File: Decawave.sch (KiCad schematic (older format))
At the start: 47 parts, among them J1 USB_OTG, J2 USART1, J3 PWR, J4 GPIO, SW1 RESET, U1 STM32L443CCTx_u, U2 MCP1700-3302E_SOT23, X1 JTAG-10

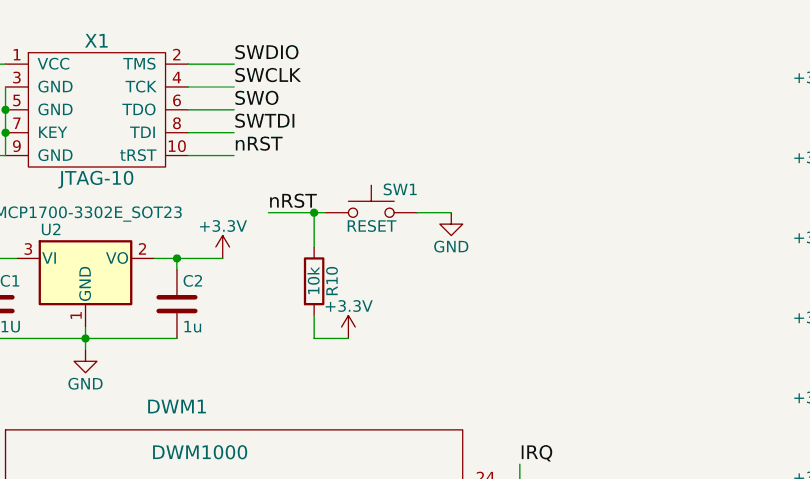
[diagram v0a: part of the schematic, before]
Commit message: adding 100n Cap for nRST
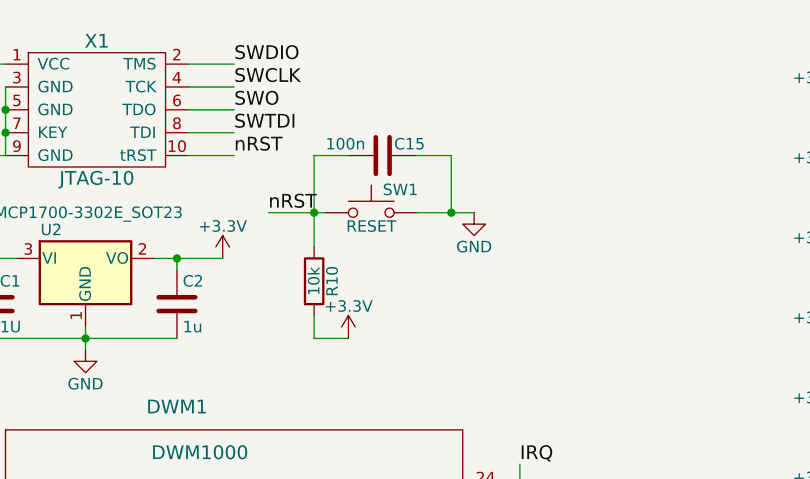
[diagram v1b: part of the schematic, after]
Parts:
- added C15: 100n, Capacitors_SMD:C_0603_HandSoldering, symbol C
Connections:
- net GND: now also C15.1
- net nRST: now also C15.2

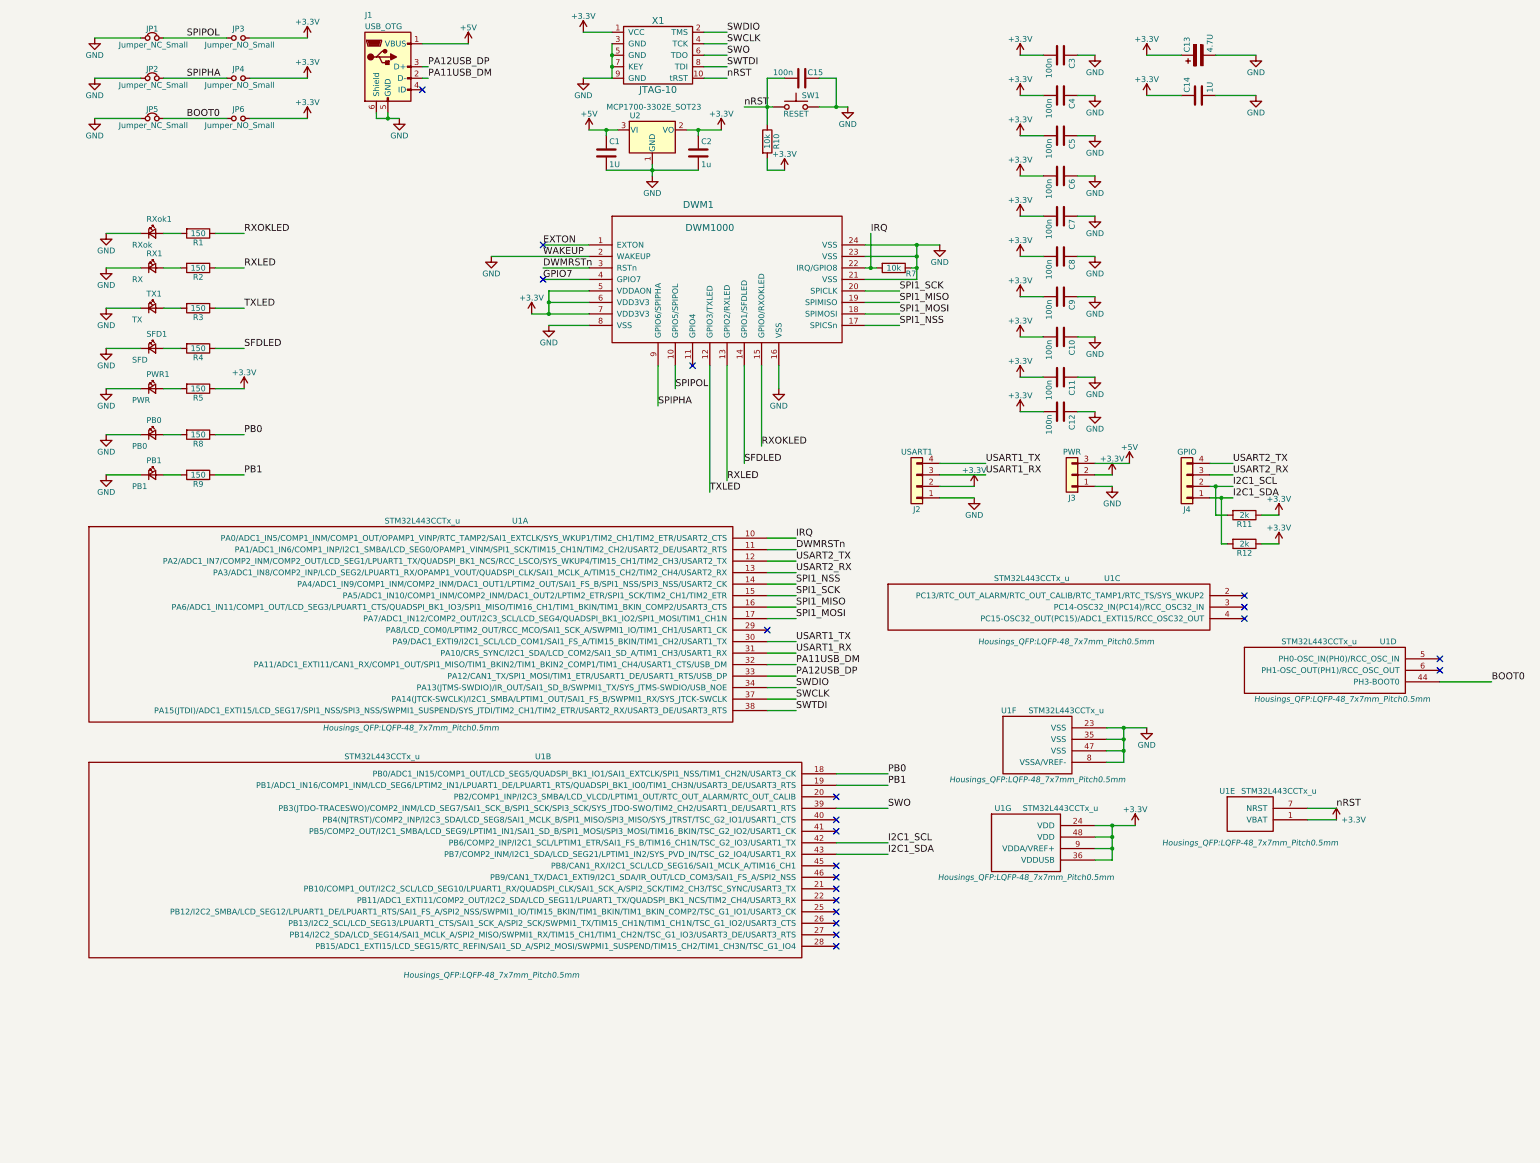
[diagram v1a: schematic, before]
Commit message: Reorganising Schematic
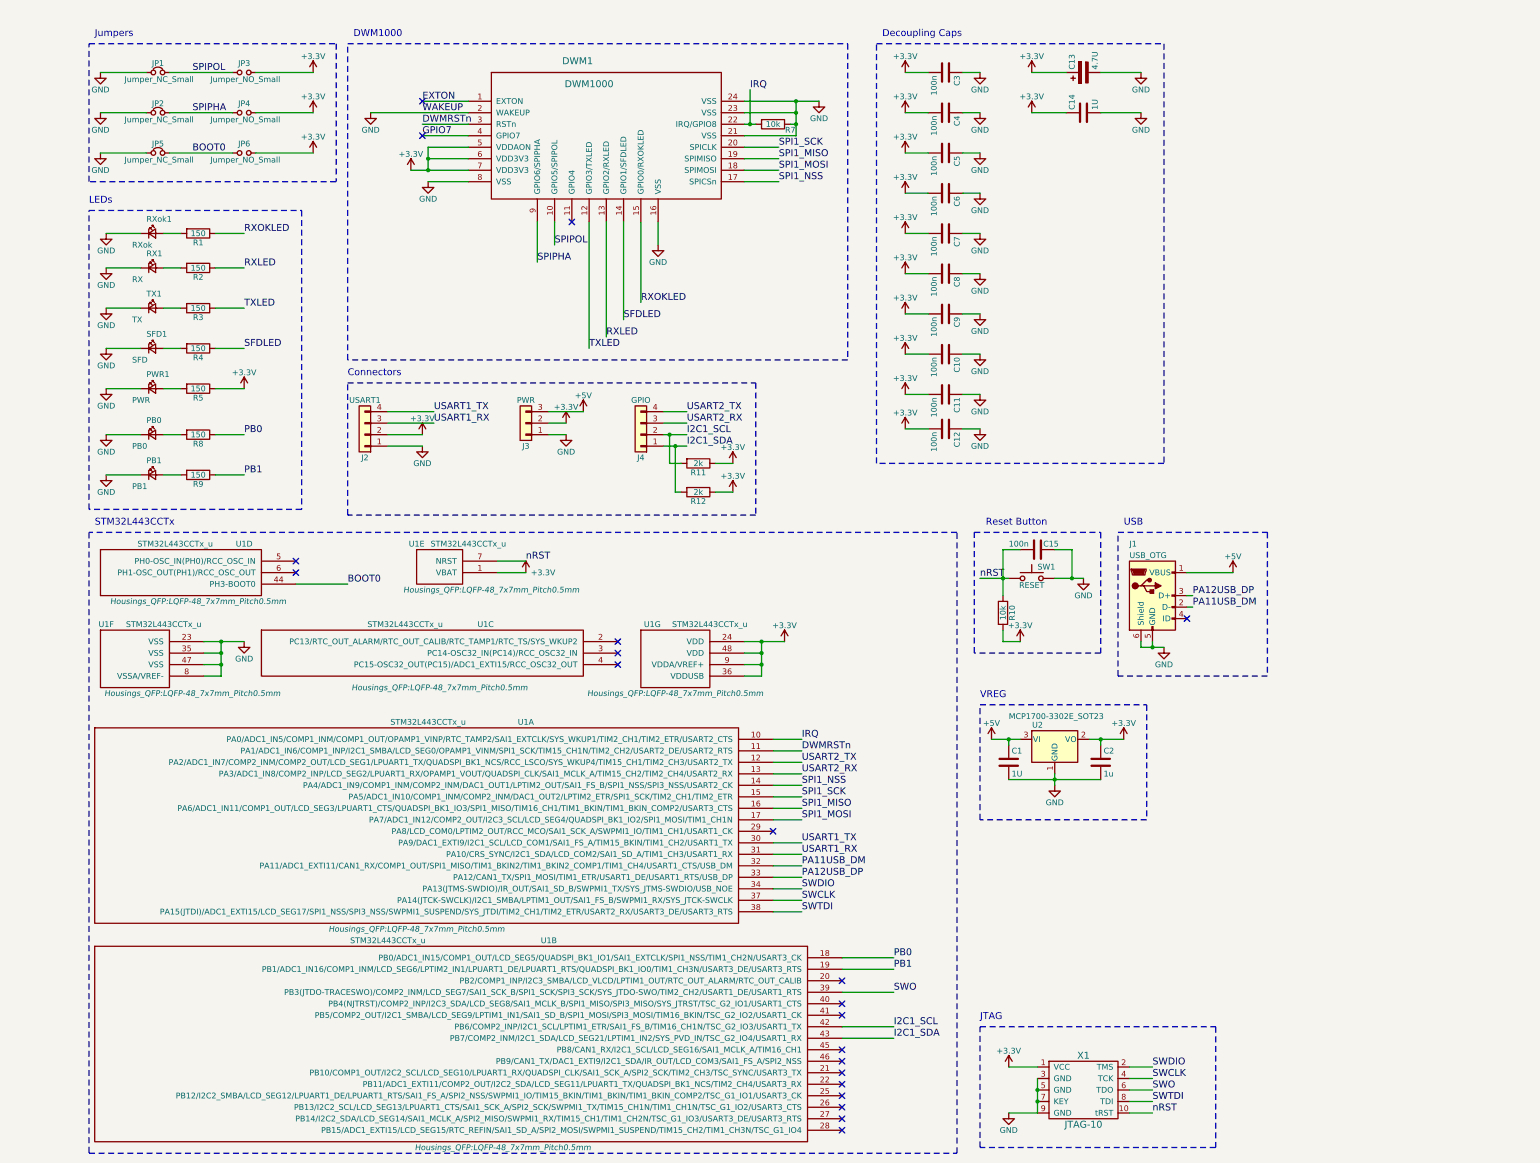
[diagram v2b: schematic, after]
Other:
- note added: "Connectors"
- note added: "DWM1000"
- note added: "Decoupling Caps"
- note added: "JTAG"
- note added: "Jumpers"
- note added: "LEDs"
- note added: "Reset Button"
- note added: "STM32L443CCTx"
- note added: "USB"
- note added: "VREG"
- moved on the sheet: C1, C10, C11, C12, C13, C14, C15, C2, C3, C4, C5, C6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

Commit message: remove unecessary jumpers
* spipol and spipha are internally pulled low by the DWM1000
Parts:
- removed JP1, JP2: Jumper_NC_Small, Resistors_SMD:R_0402, symbol Jumper_NC_Small
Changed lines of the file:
@@
-$EndComp
-$Comp
-L Jumper_NC_Small JP1
-U 1 1 59DF5453
-P 1150 1050
-F 0 "JP1" H 1150 1130 50  0000 C CNN
-F 1 "Jumper_NC_Small" H 1160 990 50  0000 C CNN
-F 2 "Resistors_SMD:R_0402" H 1150 1050 50  0001 C CNN
-F 3 "" H 1150 1050 50  0001 C CNN
-	1    1150 1050
-	1    0    0    -1
 $EndComp
 $Comp
@@
 SPIPOL
 $Comp
-L GND #PWR1
-U 1 1 59DF61DF
-P 650 1050
-F 0 "#PWR1" H 650 800 50  0001 C CNN
-F 1 "GND" H 650 900 50  0000 C CNN
-F 2 "" H 650 1050 50  0001 C CNN
-F 3 "" H 650 1050 50  0001 C CNN
-	1    650  1050
-	1    0    0    -1
-$EndComp
-$Comp
 L +3.3V #PWR12
 U 1 1 59DF61FF
@@
 $EndComp
 $Comp
-L Jumper_NC_Small JP2
-U 1 1 59DF6311
-P 1150 1400
-F 0 "JP2" H 1150 1480 50  0000 C CNN
-F 1 "Jumper_NC_Small" H 1160 1340 50  0000 C CNN
-F 2 "Resistors_SMD:R_0402" H 1150 1400 50  0001 C CNN
-F 3 "" H 1150 1400 50  0001 C CNN
-	1    1150 1400
-	1    0    0    -1
-$EndComp
-$Comp
 L Jumper_NO_Small JP4
 U 1 1 59DF6317
@@
 F 3 "" H 1900 1400 50  0001 C CNN
 	1    1900 1400
-	1    0    0    -1
-$EndComp
-$Comp
-L GND #PWR2
-U 1 1 59DF6321
-P 650 1400
-F 0 "#PWR2" H 650 1150 50  0001 C CNN
-F 1 "GND" H 650 1250 50  0000 C CNN
-F 2 "" H 650 1400 50  0001 C CNN
-F 3 "" H 650 1400 50  0001 C CNN
-	1    650  1400
 	1    0    0    -1
 $EndComp
@@
 	4450 2350 4450 2700
 Wire Wire Line
-	1250 1050 1800 1050
-Wire Wire Line
-	1050 1050 650  1050
-Wire Wire Line
 	2000 1050 2500 1050
-Wire Wire Line
-	1250 1400 1800 1400
-Wire Wire Line
-	1050 1400 650  1400
 Wire Wire Line
 	2000 1400 2500 1400
@@
 Text Notes 600  5000 0    60   ~ 0
 STM32L443CCTx
+Wire Wire Line
+	1800 1050 1450 1050
+Wire Wire Line
+	1800 1400 1450 1400
 $EndSCHEMATC

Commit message: usb footprint, route usb as differential pair
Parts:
- removed J1: USB_OTG, Connect:USB_Micro-B_10103594-0001LF, symbol USB_OTG
- added J1: 10118194-0001LF, digikey-footprints:USB_Micro_B_Female_10118194-0001LF, symbol 10118194-0001LF
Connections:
- net +5V: now also J1.1 (VBUS)
- net GND: now also J1.5 (GND), J1.6
- net PA11USB_DM renamed USBD_N
- net USBD_N: now also J1.2 (Data-)
- net PA12USB_DP renamed USBD_P
- net USBD_P: now also J1.3 (Data+)
